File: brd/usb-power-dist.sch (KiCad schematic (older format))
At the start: 37 parts, among them J1 POWER IN, J2 USB_A, J3 USB_A, J4 CASC IN, J5 CASC OUT, U1 TPS2552D, U2 TPS2552D, U3 TPS2513

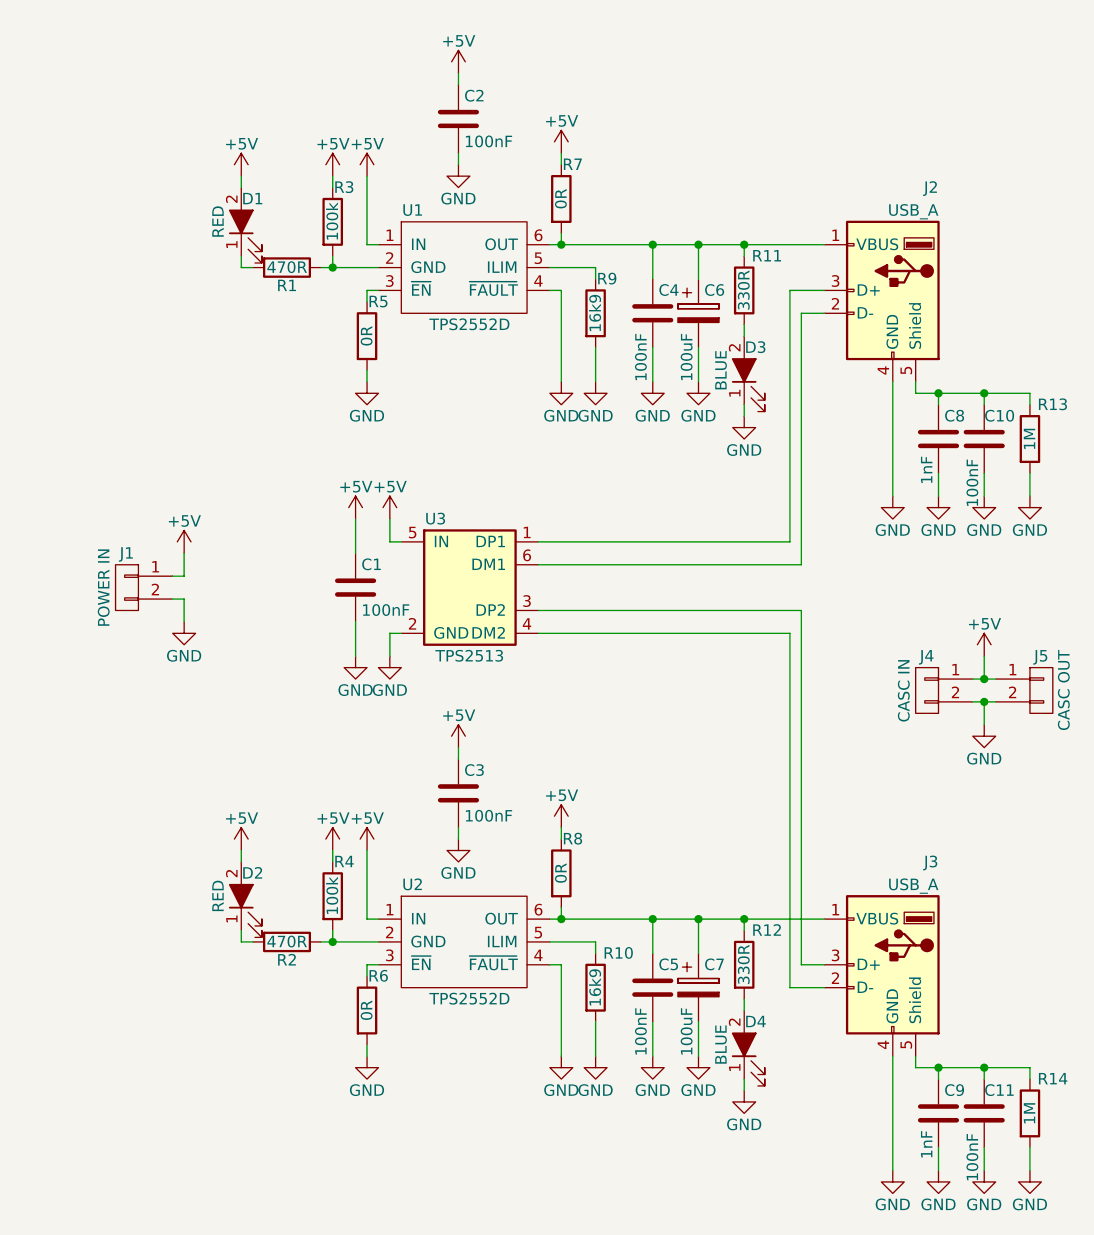
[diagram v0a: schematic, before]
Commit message: corregido esquematico por error en asignacion de pines en TPS2552, modificado valor de condensador de salida
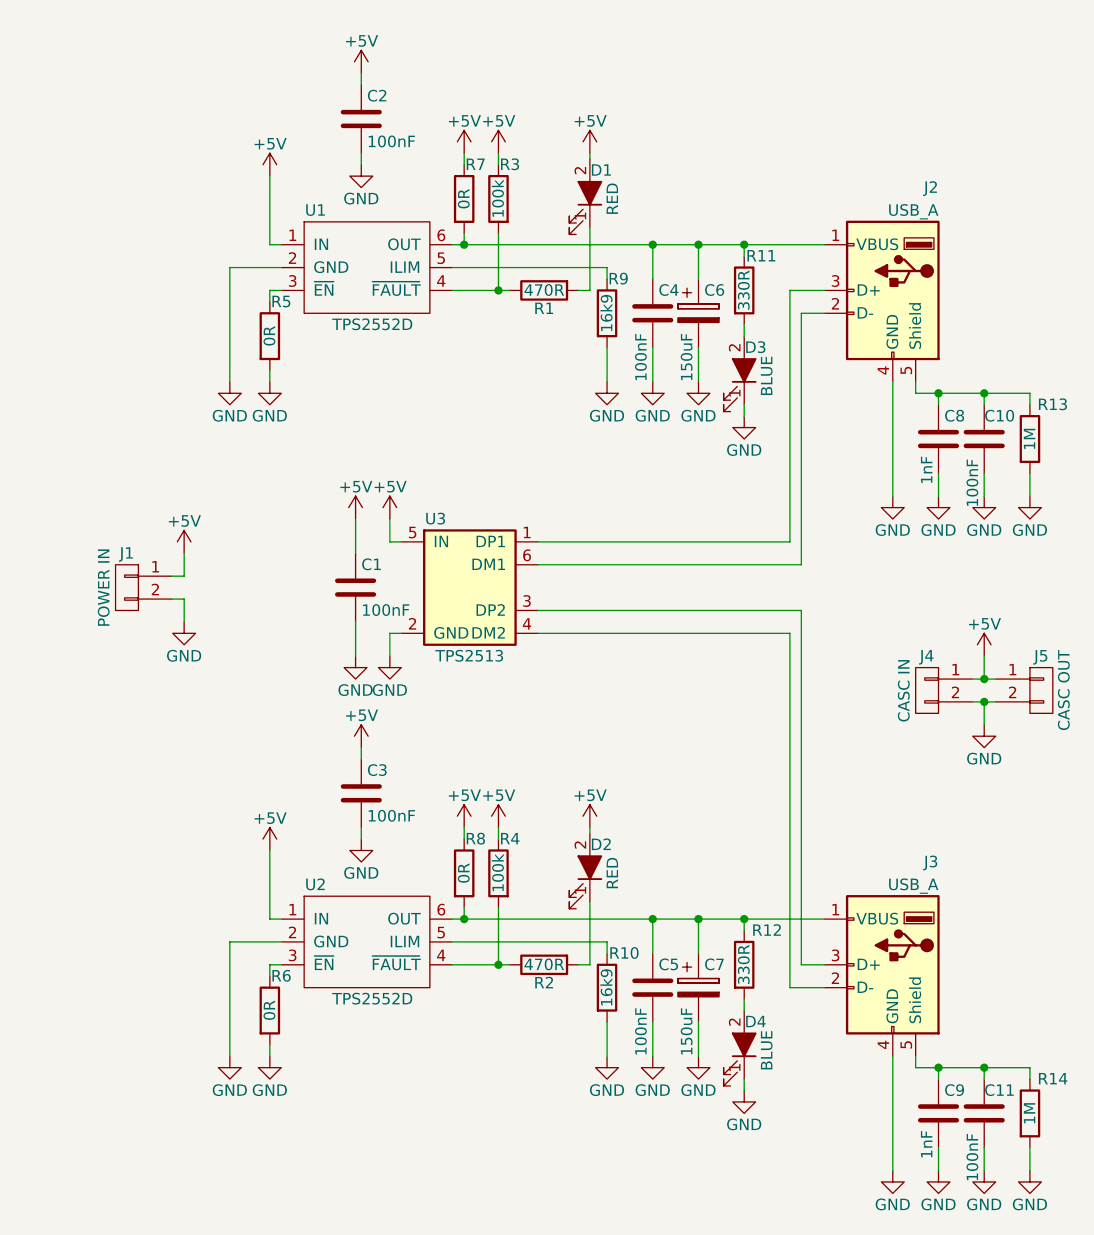
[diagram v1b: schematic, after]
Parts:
- C6, C7: value 100uF -> 150uF; footprint Capacitors_SMD:CP_Elec_6.3x5.3 -> Capacitors_SMD:CP_Elec_6.3x7.7
- J1: footprint Terminal_Blocks:TerminalBlock_Pheonix_PT-3.5mm_2pol -> Terminal_Blocks:TerminalBlock_Pheonix_MKDS1.5-2pol
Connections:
- net GND: now also U1.2 (GND), U2.2 (GND); no longer U1.4 (~FAULT), U2.4 (~FAULT)
- net at R1.1, R3.2: now also U1.4 (~FAULT); no longer U1.2 (GND)
- net at R2.1, R4.2: now also U2.4 (~FAULT); no longer U2.2 (GND)
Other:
- moved on the sheet: C2, C3, D1, D2, R1, R10, R2, R3, R4, R5, R6, R7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

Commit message: reconsideradas las opciones con respecto a ESD, EMI y shield grounding, añadidos chokes en alimentación y regenerada netlist
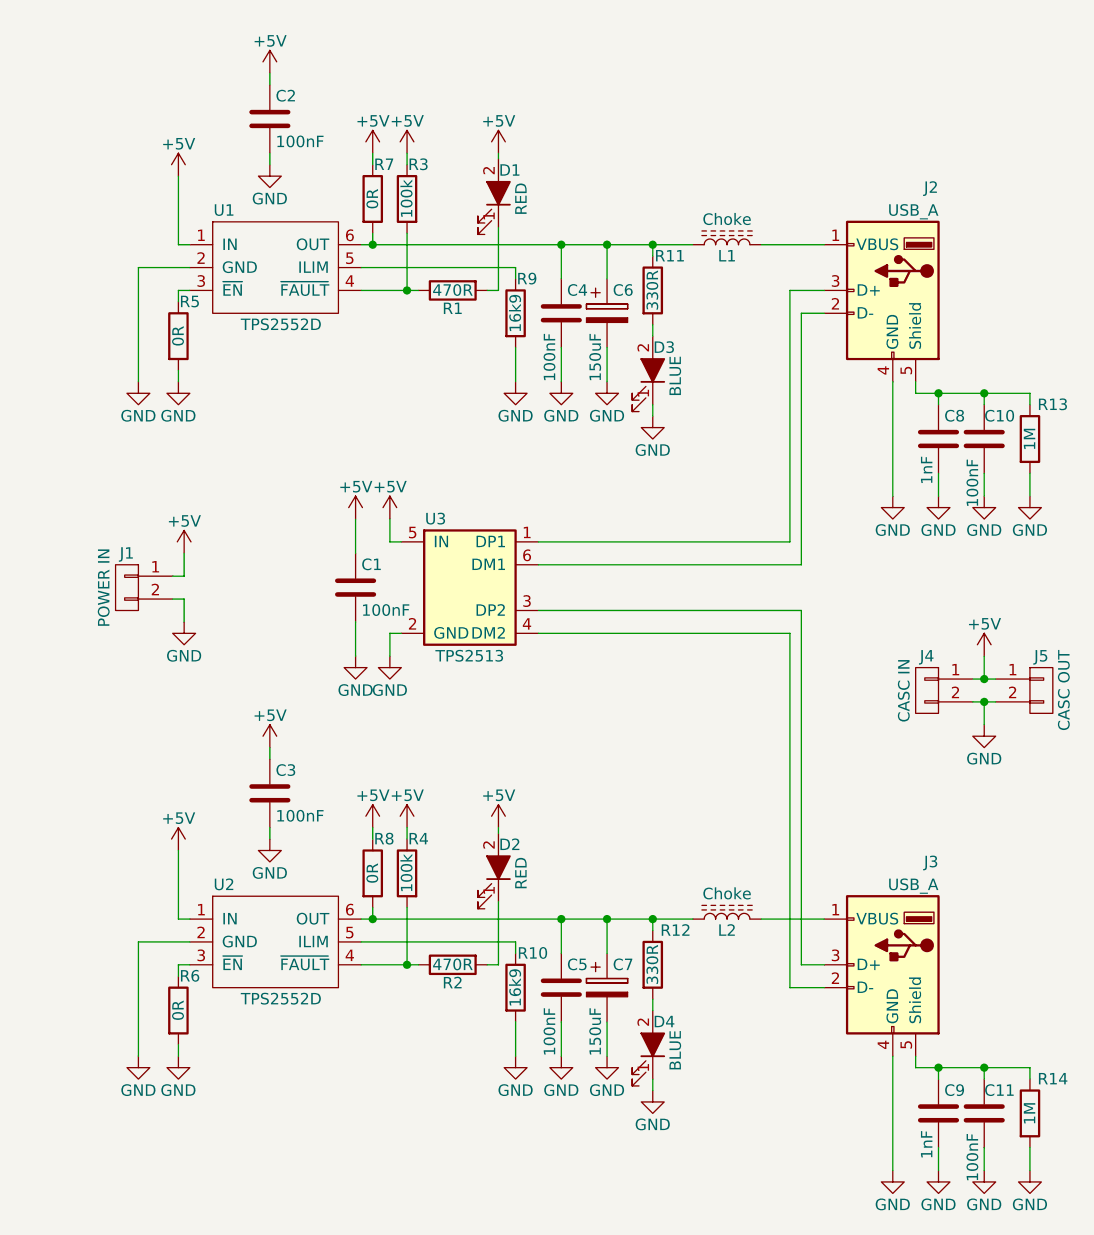
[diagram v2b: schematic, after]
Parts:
- added L1, L2: Choke, symbol L_Core_Ferrite
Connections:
- net at C4.1, C6.1, R11.1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: now also L1.1; no longer J2.1 (VBUS)
- net at C5.1, C7.1, R12.1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: now also L2.1; no longer J3.1 (VBUS)
- new net: J2.1 (VBUS), L1.2
- new net: J3.1 (VBUS), L2.2
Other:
- moved on the sheet: C2, C3, C4, C5, C6, C7, D1, D2, D3, D4, R1, R10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

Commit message: modificado el esquemático para producción (eliminadas 0R, modificados valores de componentes), añadida protección para no limitación a través PPTC, añadido BoM, renumerado esquemático
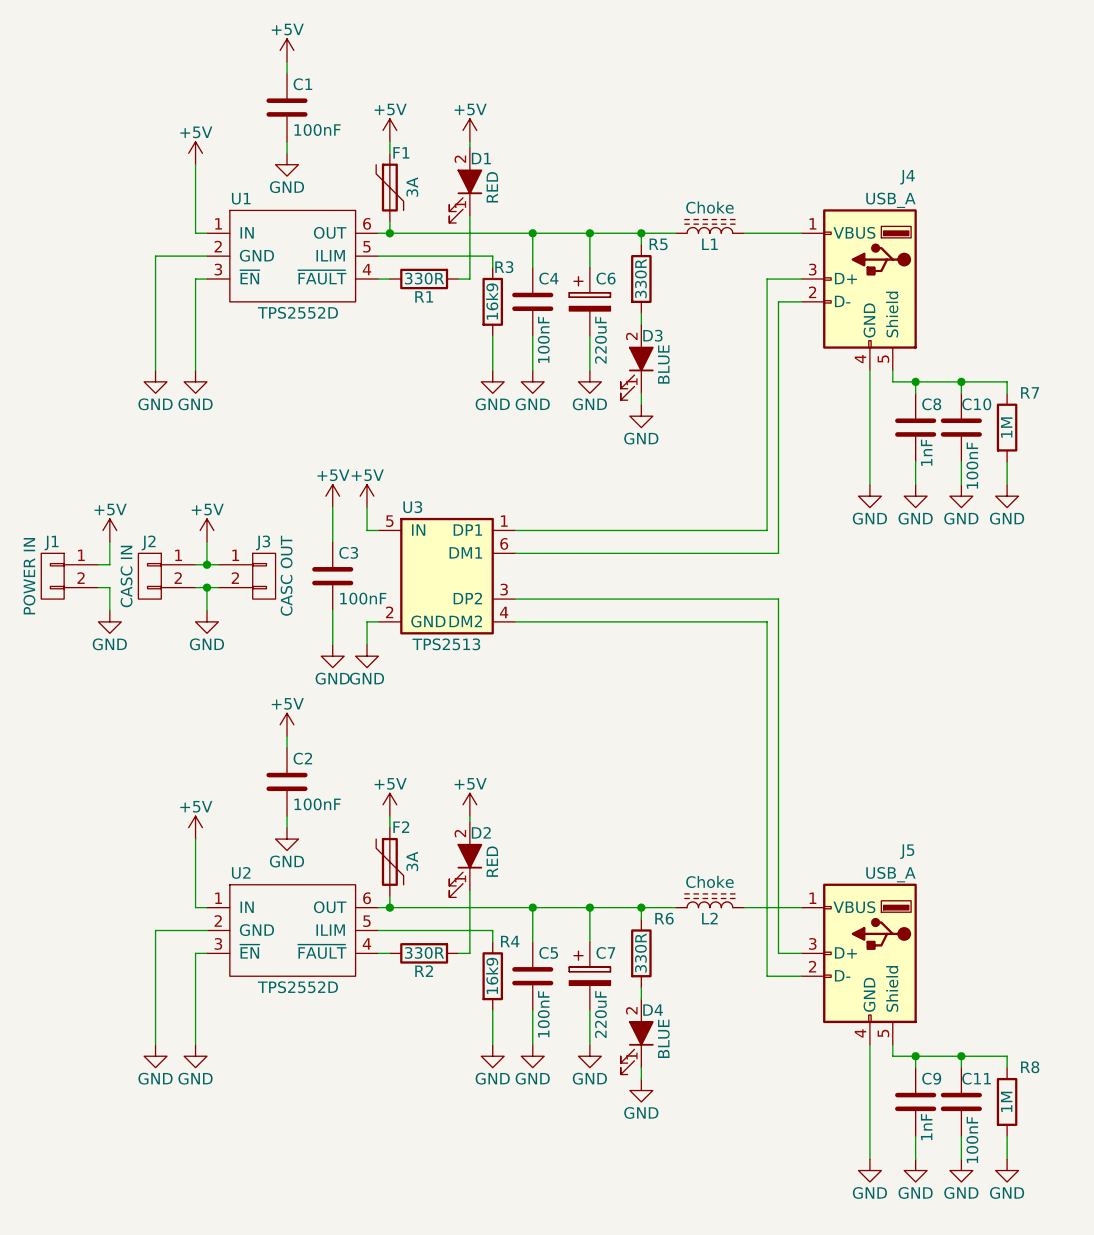
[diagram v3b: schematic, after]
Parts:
- removed R3, R4: 100k, Resistors_SMD:R_0805_HandSoldering, symbol R
- removed R5, R6, R7, R8: 0R, Resistors_SMD:R_0805_HandSoldering, symbol R
- added F1, F2: 3A, Fuse_Holders_and_Fuses:Fuse_SMD1206_Wave, symbol Polyfuse
- C1: renamed from C2; Manufacturer (none) -> Yageo; Vendor (none) -> AC0805KKX7R0BB104
- C10, C11, C4, C5: Manufacturer (none) -> Yageo; Vendor (none) -> AC0805KKX7R0BB104
- C2: renamed from C3; Manufacturer (none) -> Yageo; Vendor (none) -> AC0805KKX7R0BB104
- C3: renamed from C1; Manufacturer (none) -> Yageo; Vendor (none) -> AC0805KKX7R0BB104
- C6, C7: value 150uF -> 220uF; Manufacturer (none) -> Wurth Electronics; Vendor (none) -> 865060345007
- C8, C9: Manufacturer (none) -> Yageo; Vendor (none) -> CC0805KRX7R0BB102
- D1, D2: Manufacturer (none) -> Kingbright; Vendor (none) -> AP2012SRCPRV
- D3, D4: Manufacturer (none) -> Kingbright; Vendor (none) -> APHCM2012QBC/D-F01
- J1: Manufacturer (none) -> Phoenix Contact; Vendor (none) -> 1888687
- J4: renamed from J2; Manufacturer (none) -> Wurth Electronics; Vendor (none) -> 614004190021
- J5: renamed from J3; Manufacturer (none) -> Wurth Electronics; Vendor (none) -> 614004190021
- L1, L2: footprint (none) -> Inductors_SMD:L_0805_HandSoldering; Manufacturer (none) -> Murata Electronics; Vendor (none) -> BLM21PG121SN1D
- R1, R2: value 470R -> 330R; Manufacturer (none) -> Yageo; Vendor (none) -> RC0805JR-07330RL
- R3: renamed from R9; Manufacturer (none) -> Yageo; Vendor (none) -> RC0805FR-0716K9L
- R4: renamed from R10; Manufacturer (none) -> Yageo; Vendor (none) -> RC0805FR-0716K9L
- R5: renamed from R11; Manufacturer (none) -> Yageo; Vendor (none) -> RC0805JR-07330RL
- R6: renamed from R12; Manufacturer (none) -> Yageo; Vendor (none) -> RC0805JR-07330RL
- R7: renamed from R13; Manufacturer (none) -> Yageo; Vendor (none) -> RC0805FR-071ML
- R8: renamed from R14; Manufacturer (none) -> Yageo; Vendor (none) -> RC0805FR-071ML
- U1, U2: Manufacturer (none) -> Texas Instruments; Vendor (none) -> TPS2552DBVT
- U3: Manufacturer (none) -> Texas Instruments; Vendor (none) -> TPS2513DBVR
- renumbered J4 to J2, J5 to J3
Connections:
- net +5V: now also F1.1, F2.1
- net GND: now also U1.3 (~EN), U2.3 (~EN)
- net at C4.1, C6.1, L1.1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: now also F1.2
- net at C5.1, C7.1, L2.1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: now also F2.2
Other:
- moved on the sheet: C1, C10, C11, C2, C3, C4, C5, C6, C7, C8, C9, D1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

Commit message: renombradas nets para pistas diferenciales, regenerada netlist
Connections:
- net D1+: now reaches J4.3 (D+), U3.1 (DP1)
- net D2+: now reaches J5.3 (D+), U3.3 (DP2)
- net D2-: now reaches J5.2 (D-), U3.4 (DM2)
- net D1-: now reaches J4.2 (D-), U3.6 (DM1)
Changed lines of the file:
@@
 F 1 "TPS2552D" H 4550 1700 50  0000 C CNN
 F 2 "TO_SOT_Packages_SMD:SOT-23-6_Handsoldering" H 4150 2050 50  0001 C CNN
-F 3 "DOCUMENTATION" H 4150 2050 50  0001 C CNN
+F 3 "" H 4150 2050 50  0001 C CNN
 F 4 "TPS2552DBVT" H 4150 2050 60  0001 C CNN "Vendor"
 F 5 "Texas Instruments" H 4150 2050 60  0001 C CNN "Manufacturer"
@@
 	1    0    0    -1
 $EndComp
+Text Label 5550 3350 0    60   ~ 0
+D1+
+Text Label 5550 3450 0    60   ~ 0
+D1-
+Text Label 5550 3650 0    60   ~ 0
+D2+
+Text Label 5550 3750 0    60   ~ 0
+D2-
 $EndSCHEMATC
